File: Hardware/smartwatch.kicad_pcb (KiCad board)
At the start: 4 copper layers, 36.5 x 38 mm, 50 parts, among them IC1 W25Q256JVEIQ, IC2 NORA-B120-00B, IC3 LM66200DRLR, J3 DF37NB-24DS-0.4V51, U1 MAX17048G+T10, U11 MCP73831T-2ACI/OT, U2 TPD2EUSB30DRTR, U3 MAX30102, U4 TPS63031DSK, U5 CAM-M8C-0, U6 AP7313-18SAG-7, U7 BMI270, U8 LIS2MDLTR, U9 TPD2EUSB30DRTR, X2 9HT10-32.768KBZC-T

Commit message: -
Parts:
- added J1: Conn_01x04, Pogo_Female_4pin:Pogo_Female_4Pin, B.Cu at (138.0, 101.9)
- added J2: Conn_01x04, Pogo_Female_4pin:Pogo_Female_4Pin, B.Cu at (159.7, 102.2)
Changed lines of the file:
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@@
     (pad "" np_thru_hole circle (at 0 0 180) (size 2.1 2.1) (drill 2.1) (layers "*.Cu" "*.Mask"))
+  )
+  (footprint "Pogo_Female_4pin:Pogo_Female_4Pin" (layer "B.Cu")
+    (at 137.98 101.854 90)
+    (descr "Capacitor SMD 0402 (1005 Metric), square (rectangular) end terminal, IPC_7351 nominal, (Body size source: IPC-SM-782 page 76, https://www.pcb-3d.com/wordpress/wp-content/uploads/ipc-sm-782a_amendment_1_and_2.pdf), generated with kicad-footprint-generator")
+    (tags "capacitor")
+    (property "Sheetfile" "smartwatch.kicad_sch")
+    (property "Sheetname" "")
+    (property "ki_description" "Generic connector, single row, 01x04, script generated (kicad-library-utils/schlib/autogen/connector/)")
+    (property "ki_keywords" "connector")
+    (attr smd)
+    (fp_text reference "J1" (at 4.318 2.4892 90) (layer "B.SilkS") hide
+        (effects (font (size 1 1) (thickness 0.15)) (justify mirror))
+    )
+    (fp_text value "Conn_01x04" (at 4.468 -2.3108 90) (layer "B.Fab") hide
+        (effects (font (size 1 1) (thickness 0.15)) (justify mirror))
+    )
+    (fp_line (start -3.21 -3.85) (end 11.39 -3.85)
+      (stroke (width 0.1) (type default)) (layer "B.SilkS"))
+    (fp_line (start 11.39 3.85) (end -3.21 3.85)
+      (stroke (width 0.1) (type default)) (layer "B.SilkS"))
+    (fp_arc (start -7.06 0) (mid -5.932361 -2.722361) (end -3.21 -3.85)
+      (stroke (width 0.1) (type default)) (layer "B.SilkS"))
+    (fp_arc (start -3.21 3.85) (mid -5.932361 2.722361) (end -7.06 0)
+      (stroke (width 0.1) (type default)) (layer "B.SilkS"))
+    (fp_arc (start 11.39 -3.85) (mid 14.112361 -2.722361) (end 15.24 0)
+      (stroke (width 0.1) (type default)) (layer "B.SilkS"))
+    (fp_arc (start 15.24 0) (mid 14.112361 2.722361) (end 11.39 3.85)
+      (stroke (width 0.1) (type default)) (layer "B.SilkS"))
+    (pad "1" smd circle (at 0.244 0 90) (size 1.9 1.9) (layers "B.Cu" "B.Paste" "B.Mask")
+      (net 43 "VIN_SWD") (pinfunction "Pin_1") (pintype "passive"))
+    (pad "2" smd circle (at 2.794 0 90) (size 1.9 1.9) (layers "B.Cu" "B.Paste" "B.Mask")
+      (net 110 "/USB_N") (pinfunction "Pin_2") (pintype "passive"))
+    (pad "3" smd circle (at 5.334 0 90) (size 1.9 1.9) (layers "B.Cu" "B.Paste" "B.Mask")
+      (net 104 "/USB_P") (pinfunction "Pin_3") (pintype "passive"))
+    (pad "4" smd circle (at 7.884 0 90) (size 1.9 1.9) (layers "B.Cu" "B.Paste" "B.Mask")
+      (net 1 "GND") (pinfunction "Pin_4") (pintype "passive"))
+    (model "${KICAD6_3DMODEL_DIR}/Capacitor_SMD.3dshapes/C_0402_1005Metric.wrl"
+      (offset (xyz 0 0 0))
+      (scale (xyz 1 1 1))
+      (rotate (xyz 0 0 0))
+    )
+  )
+  (footprint "Pogo_Female_4pin:Pogo_Female_4Pin" (layer "B.Cu")
+    (at 159.69 102.204 90)
+    (descr "Capacitor SMD 0402 (1005 Metric), square (rectangular) end terminal, IPC_7351 nominal, (Body size source: IPC-SM-782 page 76, https://www.pcb-3d.com/wordpress/wp-content/uploads/ipc-sm-782a_amendment_1_and_2.pdf), generated with kicad-footprint-generator")
+    (tags "capacitor")
+    (property "Sheetfile" "smartwatch.kicad_sch")
+    (property "Sheetname" "")
+    (property "ki_description" "Generic connector, single row, 01x04, script generated (kicad-library-utils/schlib/autogen/connector/)")
+    (property "ki_keywords" "connector")
+    (attr smd)
+    (fp_text reference "J2" (at 4.318 2.4892 90) (layer "B.SilkS") hide
+        (effects (font (size 1 1) (thickness 0.15)) (justify mirror))
+    )
+    (fp_text value "Conn_01x04" (at 4.468 -2.3108 90) (layer "B.Fab") hide
+        (effects (font (size 1 1) (thickness 0.15)) (justify mirror))
+    )
+    (fp_line (start -3.21 -3.85) (end 11.39 -3.85)
+      (stroke (width 0.1) (type default)) (layer "B.SilkS"))
+    (fp_line (start 11.39 3.85) (end -3.21 3.85)
+      (stroke (width 0.1) (type default)) (layer "B.SilkS"))
+    (fp_arc (start -7.06 0) (mid -5.932361 -2.722361) (end -3.21 -3.85)
+      (stroke (width 0.1) (type default)) (layer "B.SilkS"))
+    (fp_arc (start -3.21 3.85) (mid -5.932361 2.722361) (end -7.06 0)
+      (stroke (width 0.1) (type default)) (layer "B.SilkS"))
+    (fp_arc (start 11.39 -3.85) (mid 14.112361 -2.722361) (end 15.24 0)
+      (stroke (width 0.1) (type default)) (layer "B.SilkS"))
+    (fp_arc (start 15.24 0) (mid 14.112361 2.722361) (end 11.39 3.85)
+      (stroke (width 0.1) (type default)) (layer "B.SilkS"))
+    (pad "1" smd circle (at 0.244 0 90) (size 1.9 1.9) (layers "B.Cu" "B.Paste" "B.Mask")
+      (net 43 "VIN_SWD") (pinfunction "Pin_1") (pintype "passive"))
+    (pad "2" smd circle (at 2.794 0 90) (size 1.9 1.9) (layers "B.Cu" "B.Paste" "B.Mask")
+      (net 61 "/SWDIO") (pinfunction "Pin_2") (pintype "passive"))
+    (pad "3" smd circle (at 5.334 0 90) (size 1.9 1.9) (layers "B.Cu" "B.Paste" "B.Mask")
+      (net 64 "/SWDCLK") (pinfunction "Pin_3") (pintype "passive"))
+    (pad "4" smd circle (at 7.884 0 90) (size 1.9 1.9) (layers "B.Cu" "B.Paste" "B.Mask")
+      (net 1 "GND") (pinfunction "Pin_4") (pintype "passive"))
+    (model "${KICAD6_3DMODEL_DIR}/Capacitor_SMD.3dshapes/C_0402_1005Metric.wrl"
+      (offset (xyz 0 0 0))
+      (scale (xyz 1 1 1))
+      (rotate (xyz 0 0 0))
+    )
   )
   (gr_arc (start 148.97 78.73) (mid 160.341996 82.509037) (end 167.190287 92.342872)

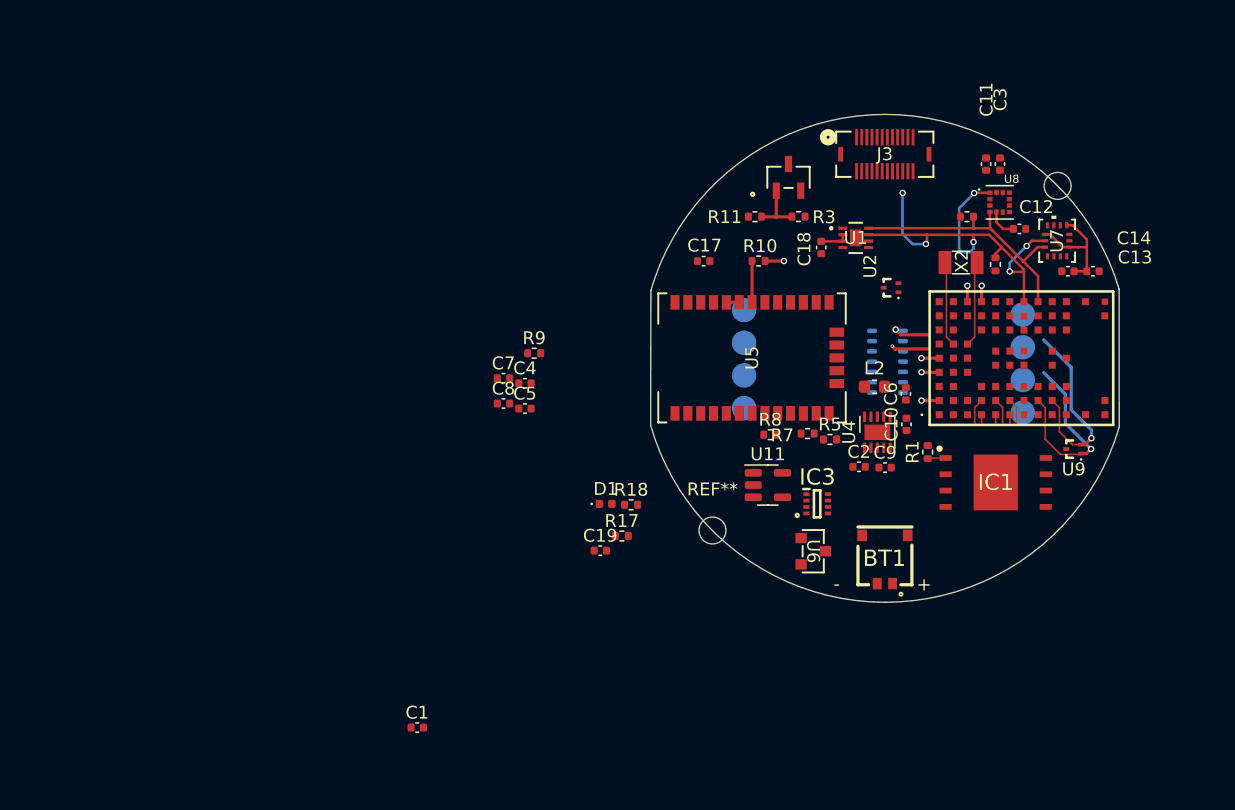
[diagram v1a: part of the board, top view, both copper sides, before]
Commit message: changed gps moduleto l96
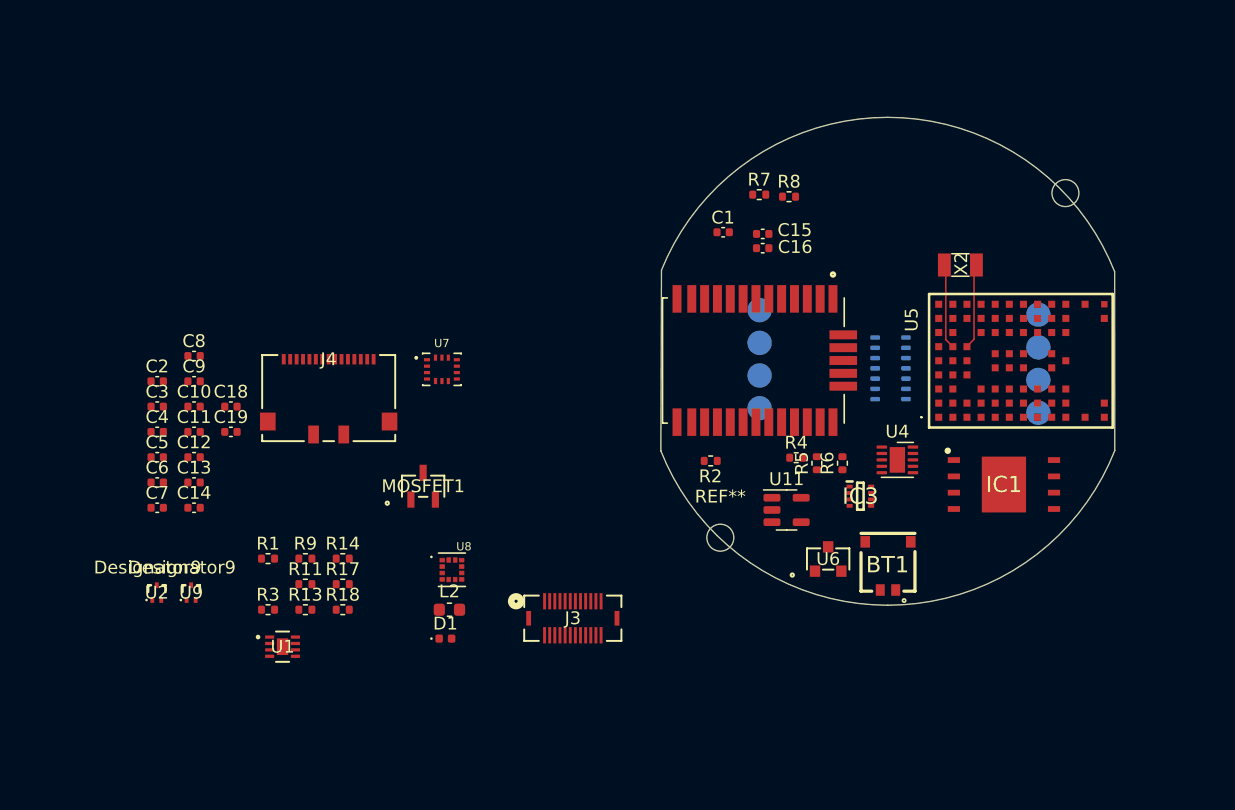
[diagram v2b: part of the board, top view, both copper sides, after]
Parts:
- removed C17: 4.7uF, Capacitor_SMD:C_0402_1005Metric
- removed R10: 220, Resistor_SMD:R_0402_1005Metric
- added C15: 100nF, Capacitor_SMD:C_0402_1005Metric, F.Cu at (139.4, 88.0)
- added C16: 4.7uF, Capacitor_SMD:C_0402_1005Metric, F.Cu at (139.4, 89.2)
- added J4: 5022441530, MOLEX_5022441530:CONN_502244-1530_MOL, F.Cu at (105.6, 100.8)
- added R2: 0R, Resistor_SMD:R_0402_1005Metric, F.Cu at (135.4, 105.7)
- added R4: 1k, Resistor_SMD:R_0402_1005Metric, F.Cu at (142.0, 105.5)
- added R6: 1k, Resistor_SMD:R_0402_1005Metric, F.Cu at (145.6, 105.9)
- C1: value 1uF -> 10uF
- C12: value 10u -> 220nF
- R5, R8: value 220 -> 5k6
- R7: value 220 -> 1k
- U5: value CAM-M8C-0 -> L96-M33; footprint CAM-M8C:QFN_M8C-0_UBL -> L96-M33:XCVR_L96-M33
- U7: footprint BMI270:BMI270_BOS -> BMI270:XDCR_BMI270
- moved C14 72.4 mm to (95.1, 109.4)
- moved C13 70.0 mm to (95.1, 107.4), turned to 0 degrees
- moved U9 69.6 mm to (94.9, 116.0), turned to 0 degrees
- moved C3 68.3 mm to (92.3, 101.5), turned to 0 degrees
- moved C12 66.7 mm to (95.1, 105.4)
- moved C11 65.1 mm to (95.1, 103.5), turned to 0 degrees
- moved U2 61.9 mm to (92.2, 116.0), turned to 0 degrees
- moved R13 59.9 mm to (103.8, 117.3), turned to 0 degrees
- moved C6 58.7 mm to (92.3, 107.4), turned to 0 degrees
- moved R14 55.8 mm to (106.7, 113.3), turned to 0 degrees
- moved C10 55.5 mm to (95.1, 101.5), turned to 0 degrees
- moved C2 55.1 mm to (92.3, 99.5)
- moved U1 54.8 mm to (102.0, 120.2)
- moved C9 54.2 mm to (95.1, 99.5)
- moved R1 52.0 mm to (100.9, 113.3), turned to 0 degrees
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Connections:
- C1 pad 1: Net-(D1-A) -> +3.3V
- IC2 pad G4: unconnected-(IC2-P1.04-PadG4) -> /BAT_INT
- R13 pad 2: +3.3V -> +1V8
- R14 pad 2: +3.3V -> +1V8
- R5 pad 1: Net-(R5-Pad1) -> GND
- R5 pad 2: /GPS_TX -> Net-(U5-RXD1)
- R7 pad 1: Net-(R7-Pad1) -> /GPS_EXTINT
- R7 pad 2: /GPS_RX -> Net-(U5-EXTINT0)
- R8 pad 1: Net-(R8-Pad1) -> GND
- R8 pad 2: /GPS_RESET -> Net-(U5-EXTINT0)
- U1 pad 5: unconnected-(U1-*ALRT-Pad5) -> /BAT_INT
- U5 pad 1: +3.3V -> (no net)
- U5 pad 16: Net-(U5-Pad16) -> Net-(U5-RF_OUT)
- U5 pad 17: Net-(U5-Pad16) -> Net-(U5-RF_IN)
- U5 pad 23: Net-(R8-Pad1) -> unconnected-(U5-~{RESET}-Pad23)
- U5 pad 25: Net-(R7-Pad1) -> Net-(U5-TXD1)
- U5 pad 26: Net-(R5-Pad1) -> Net-(U5-RXD1)
- U5 pad 7: Net-(R10-Pad2) -> Net-(U5-EXTINT0)
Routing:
- net /SCL: track 36.5 -> 0.00 mm, vias 6 -> 0
- net /SDA: track 21.1 -> 0.00 mm
- net /SWDCLK: track 15.0 -> 0.00 mm, vias 1 -> 0
- net /SWDIO: track 15.0 -> 0.00 mm, vias 1 -> 0
- net +1V8: track 9.17 -> 0.00 mm
- net Net-(MOSFET1-G): track 4.39 -> 0.00 mm
- net Net-(R10-Pad2): track 3.22 -> 0.00 mm
- net unconnected-(IC2-N/C_1-PadA6): track 2.89 -> 0.00 mm, vias 1 -> 0
- net unconnected-(U3-NC-Pad1): track 2.71 -> 0.00 mm, vias 1 -> 0
- net Net-(U8-C1): track 2.32 -> 0.00 mm
- net /FLASH_CS: track 2.23 -> 0.00 mm
- net /BAT+: track 2.19 -> 0.00 mm
- net /FLASH_IO1: track 2.13 -> 0.00 mm
- net /FLASH_IO3: track 2.12 -> 0.00 mm
- net /FLASH_IO0: track 2.11 -> 0.00 mm
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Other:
- board size 36.5 x 38 mm -> 35.4 x 38 mm
- board text removed: "+"
- board text removed: "-"

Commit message: -
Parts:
- removed J4: 5022441530, MOLEX_5022441530:CONN_502244-1530_MOL
- removed the REF** at (136.1, 111.7)
- removed the REF** at (163.0, 84.9)
- added REF**: MountingHole_2.2mm_M2, MountingHole:MountingHole_2.2mm_M2, F.Cu at (159.3, 117.6)
- added REF**: MountingHole_2.2mm_M2, MountingHole:MountingHole_2.2mm_M2, F.Cu at (159.3, 79.0)
- moved U9 80.5 mm to (174.8, 106.2)
- moved U2 72.8 mm to (160.6, 91.1), turned to -90 degrees
- moved U1 72.6 mm to (163.7, 81.9)
- moved C2 70.9 mm to (162.7, 107.4), turned to 90 degrees
- moved C6 67.0 mm to (159.2, 104.3), turned to 180 degrees
- moved C9 66.5 mm to (161.0, 108.9)
- moved C10 64.1 mm to (159.2, 103.2), turned to 180 degrees
- moved U8 59.6 mm to (167.2, 85.1)
- moved U7 57.3 mm to (170.8, 88.6)
- moved C19 56.5 mm to (153.5, 114.3)
- moved J3 47.1 mm to (159.6, 86.3)
- moved MOSFET1 46.0 mm to (152.0, 83.3)
- moved L2 43.6 mm to (157.3, 106.8), turned to -90 degrees
- moved R17 40.2 mm to (146.6, 110.0)
- moved C11 36.7 mm to (131.5, 108.4)
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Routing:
- net Net-(U4-EN): track 0.00 -> 2.42 mm
- net Net-(U4-L2): track 0.00 -> 2.15 mm
- net Net-(U4-L1): track 0.00 -> 1.71 mm
- net VIN_SWD: track 0.00 -> 1.44 mm, vias 0 -> 1
- net /BAT+: track 0.00 -> 1.42 mm, vias 0 -> 1
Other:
- board size 35.4 x 38 mm -> 35 x 38.6 mm

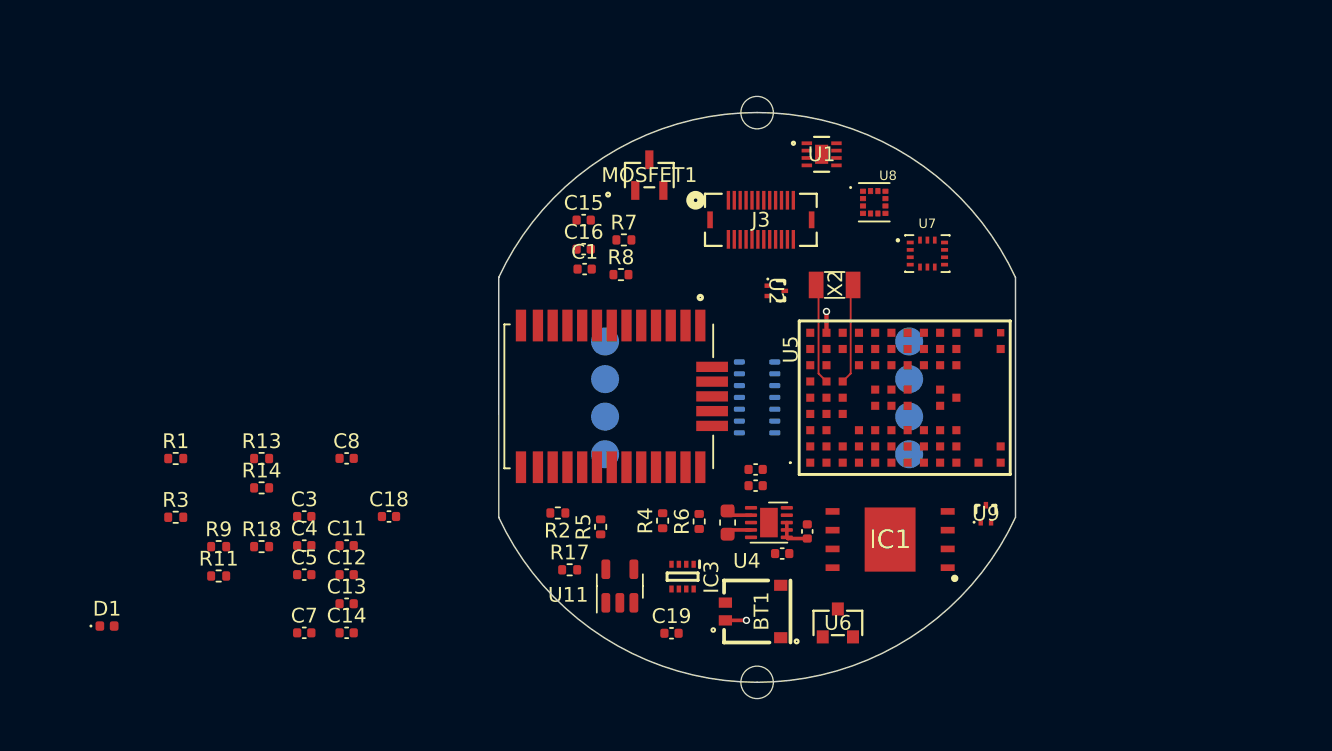
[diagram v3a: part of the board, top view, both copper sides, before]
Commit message: added rtc
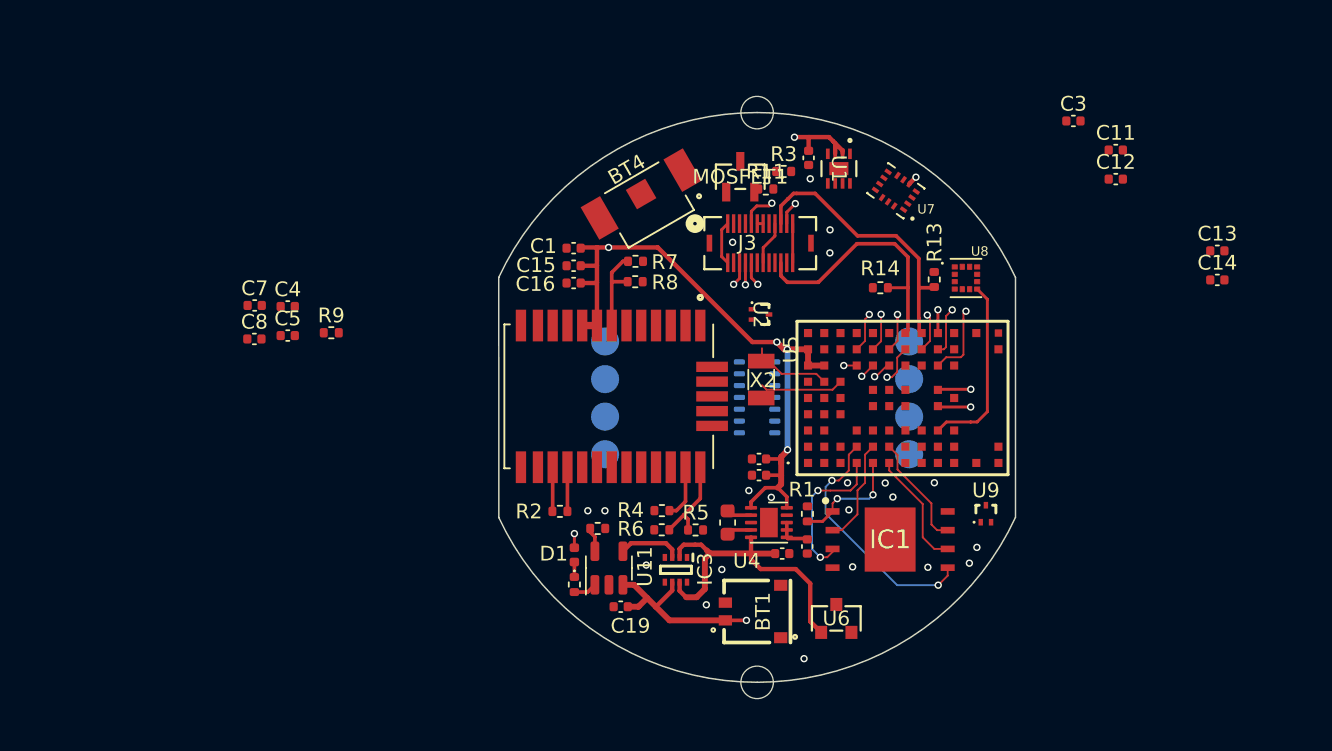
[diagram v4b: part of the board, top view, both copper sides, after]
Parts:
- added BT4: 2994TR, 2994TR:BAT_2994TR, F.Cu at (151.4, 84.5)
- moved C13 63.7 mm to (190.5, 88.4)
- moved C14 63.7 mm to (190.5, 90.4)
- moved C11 58.6 mm to (183.6, 81.6)
- moved C12 58.6 mm to (183.6, 83.5)
- moved C3 58.6 mm to (180.7, 79.6)
- moved R3 47.4 mm to (161.1, 83.0)
- moved R13 47.2 mm to (171.3, 90.3), turned to 90 degrees
- moved R11 45.4 mm to (159.9, 84.2)
- moved R14 44.1 mm to (167.7, 90.9), turned to 180 degrees
- moved R1 43.0 mm to (162.7, 106.2), turned to 90 degrees
- moved C18 37.4 mm to (162.8, 82.1), turned to -90 degrees
- moved D1 32.0 mm to (146.9, 109.0), turned to 90 degrees
- moved C7 22.4 mm to (125.3, 92.1)
- moved R18 21.3 mm to (146.9, 111.0), turned to 90 degrees
- moved R9 16.4 mm to (130.4, 93.9)
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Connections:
- IC2 pad A2: /GPS_RESET -> /GPS_EXTINT
- IC2 pad J3: unconnected-(IC2-RESET_N-PadJ3) -> /LIS2MDLTR_INT
- IC2 pad J4: unconnected-(IC2-N/C_3-PadJ4) -> /INT1_BMI270
- IC2 pad J5: unconnected-(IC2-N/C_4-PadJ5) -> /INT2_BMI270
- U5 pad 8: +3.3V -> RTC Battery
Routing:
- net +3.3V: track 0.00 -> 51.2 mm, vias 0 -> 4
- net VBUS: track 0.00 -> 22.5 mm
- net /SDA: track 0.00 -> 18.9 mm
- net /SCL: track 0.00 -> 17.7 mm
- net /BAT+: track 1.42 -> 18.5 mm, vias 1 -> 2
- net /FLASH_IO0: track 0.00 -> 16.8 mm, vias 0 -> 2
- net /LIS2MDLTR_INT: track 0.00 -> 12.5 mm
- net /FLASH_IO2: track 0.00 -> 10.4 mm, vias 0 -> 2
- net /FLASH_CLK: track 0.00 -> 8.00 mm
- net /FLASH_IO3: track 0.00 -> 7.72 mm
- net /FLASH_CS: track 0.00 -> 7.67 mm, vias 0 -> 2
- net /FLASH_IO1: track 0.00 -> 7.15 mm
- net Net-(U5-RXD1): track 0.00 -> 6.21 mm
- net Net-(U5-EXTINT0): track 0.00 -> 6.08 mm
- net /RTC_INT: track 0.00 -> 5.05 mm, vias 0 -> 1
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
